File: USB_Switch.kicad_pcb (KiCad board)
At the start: 2 copper layers, 42 x 61 mm, 30 parts, among them J1 Conn_01x06, J2 USB_IN, J3 USB_OUT, J4 Conn_01x08, J5 USB_OUT, Q1 Q_NMOS_GDS, Q2 Q_NMOS_GDS, SW1 PRGM, U1 AMS1117-3.3, U2 INA219AxD, U3 INA219AxD, U4 ESP-12F

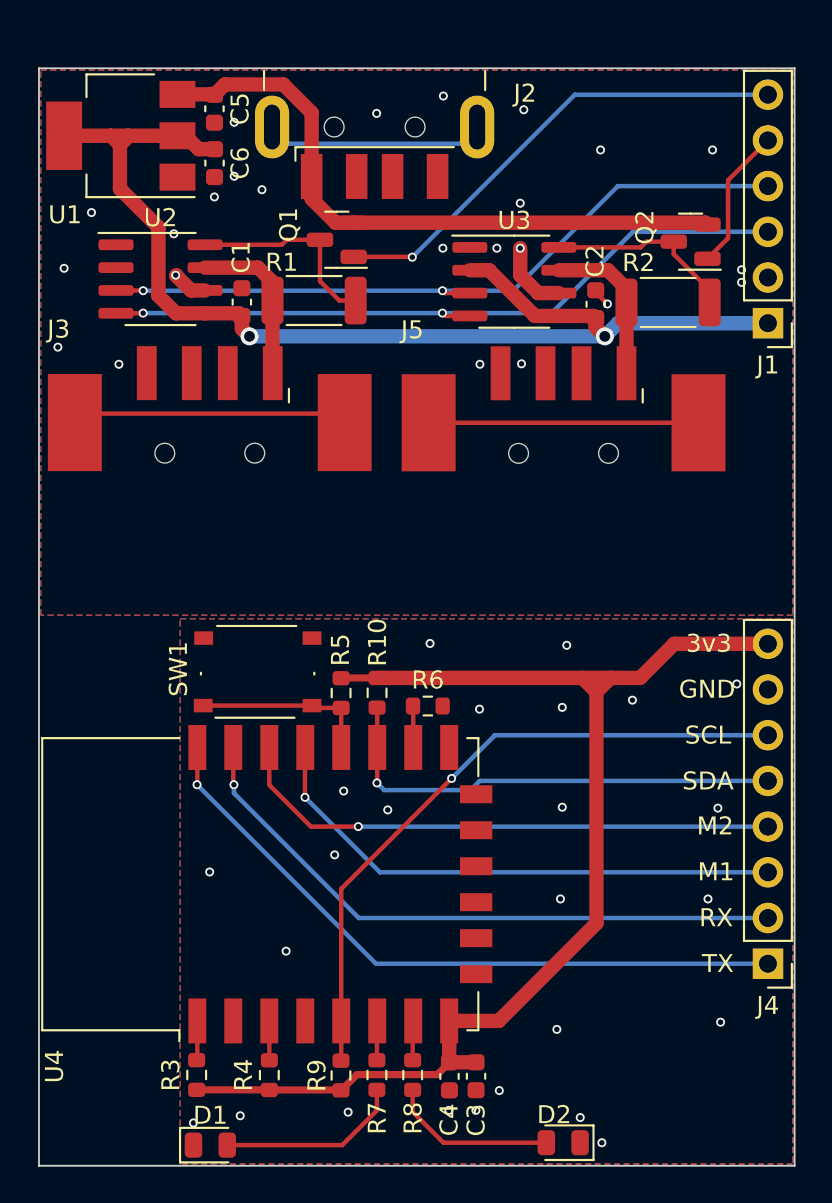
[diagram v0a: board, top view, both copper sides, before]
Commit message: Fixed inversed naming on connectors
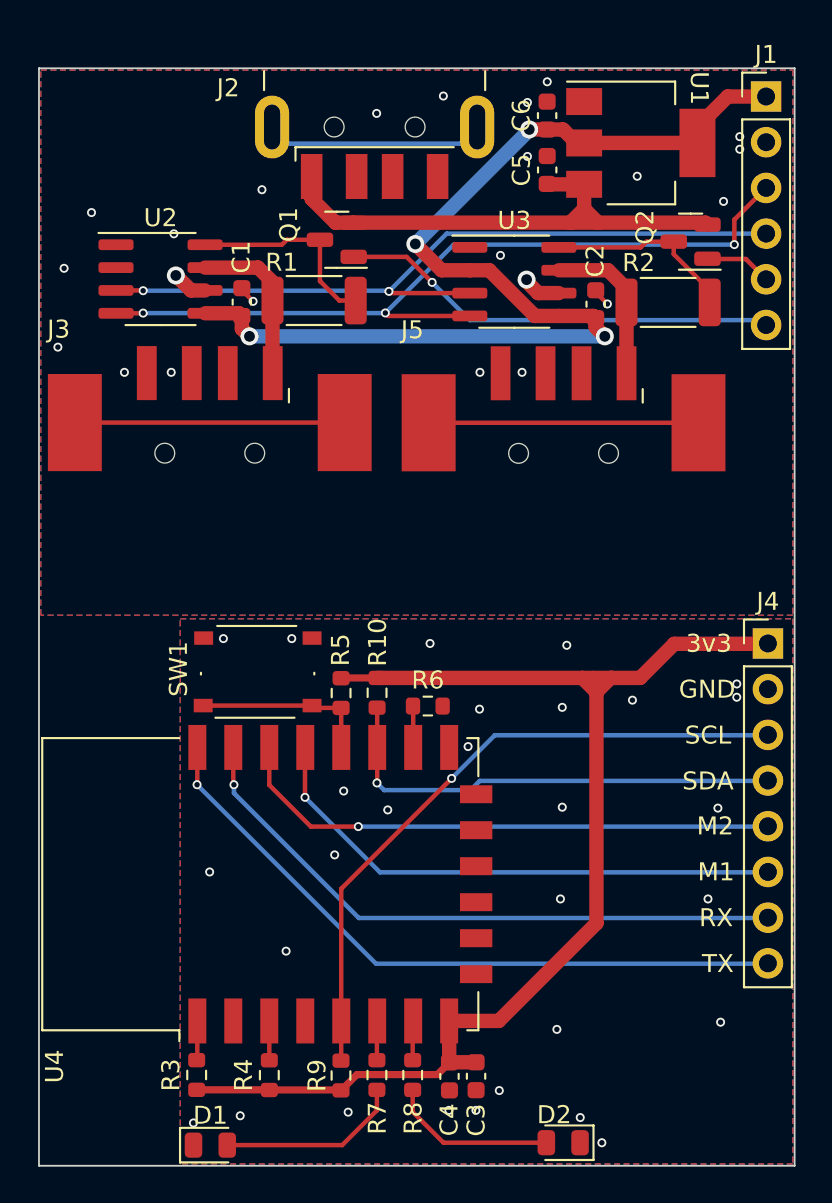
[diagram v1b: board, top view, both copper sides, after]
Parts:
- moved U1 28.9 mm to (69.0, 86.5), turned to 0 degrees
- moved C5 18.8 mm to (63.8, 88.0), turned to 90 degrees
- moved C6 18.7 mm to (63.8, 85.0), turned to 90 degrees
- moved J4 17.8 mm to (76.0, 114.3), turned to 0 degrees
- moved J1 12.6 mm to (76.0, 83.9), turned to 0 degrees
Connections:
- J4 pad 1: /Control Board/C_TX -> /Control Board/C_3v3
- J4 pad 2: /Control Board/C_RX -> GND
- J4 pad 3: /Control Board/M1_TOGGLE -> /Control Board/C_I2C_SCL
- J4 pad 4: /Control Board/M2_TOGGLE -> /Control Board/C_I2C_SDA
- J4 pad 5: /Control Board/C_I2C_SDA -> /Control Board/M2_TOGGLE
- J4 pad 6: /Control Board/C_I2C_SCL -> /Control Board/M1_TOGGLE
- J4 pad 7: GND -> /Control Board/C_RX
- J4 pad 8: /Control Board/C_3v3 -> /Control Board/C_TX
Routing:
- net /MOSFET Board/5V_IN: track 35.7 -> 29.4 mm
- net /MOSFET Board/M_I2C_SCL: track 39.7 -> 44.6 mm, vias 2 -> 3
- net /MOSFET Board/M2_TOGGLE: track 7.97 -> 3.73 mm
- net /MOSFET Board/M_3v3: track 64.2 -> 60.2 mm, vias 2 -> 4
- net /MOSFET Board/M1_TOGGLE: track 26.8 -> 24.5 mm
- net /MOSFET Board/M_I2C_SDA: track 40.2 -> 42.0 mm
- net GND: track 7.06 -> 6.13 mm, vias 49 -> 52

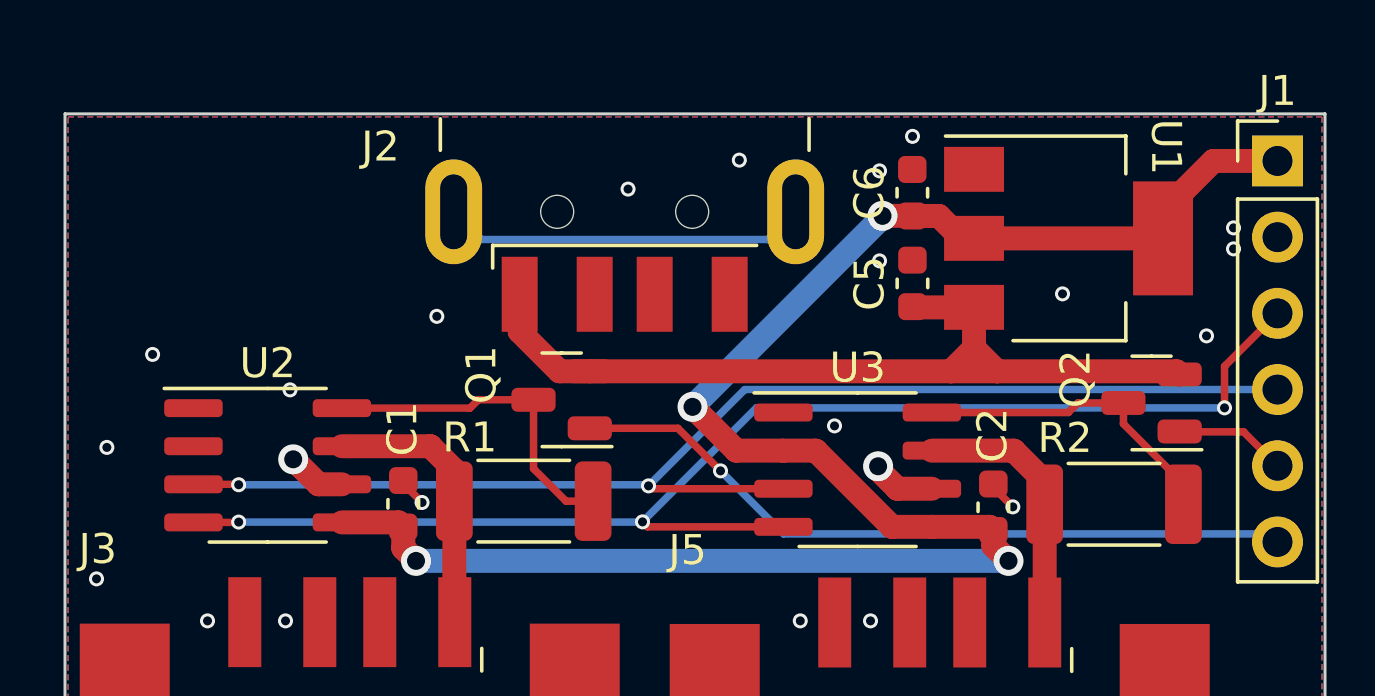
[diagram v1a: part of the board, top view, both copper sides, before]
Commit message: Added more GND vias, fixed incorrect net trace sizing
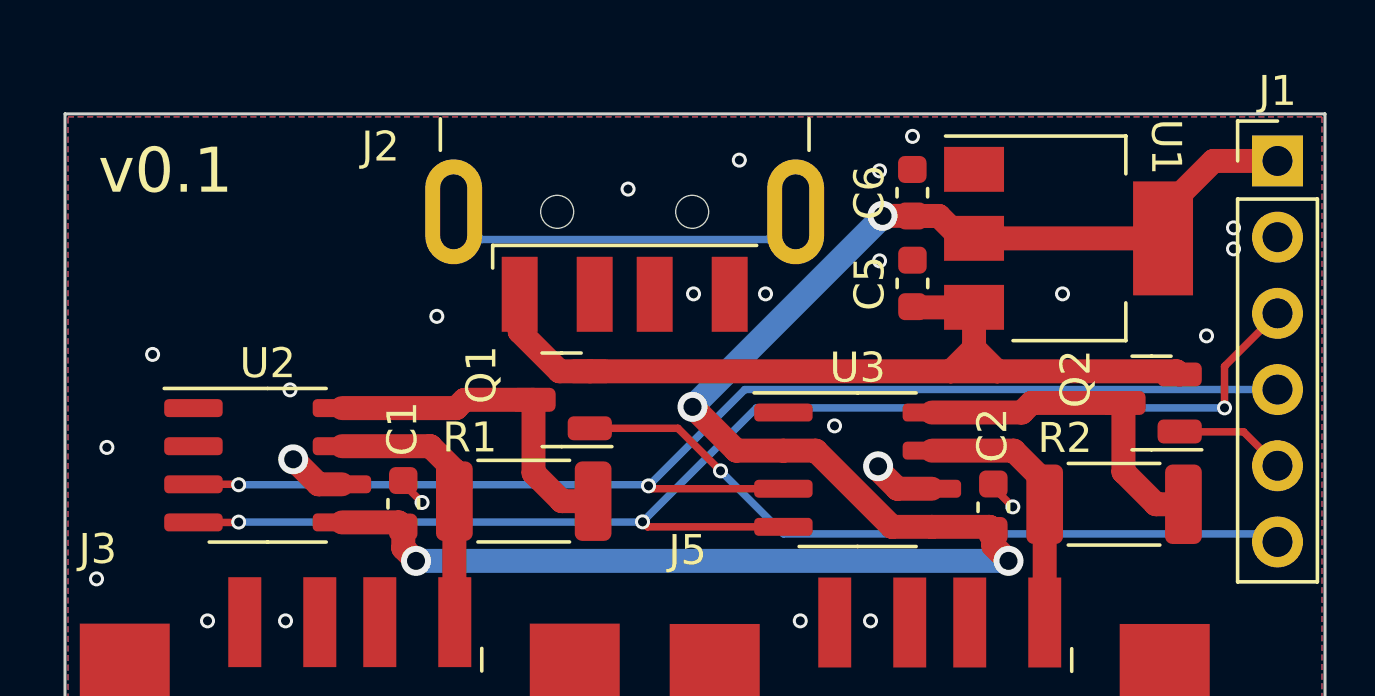
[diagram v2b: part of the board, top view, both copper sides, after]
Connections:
- net Net-(Q1-Pad3) renamed /MOSFET Board/5V_PRER_1
- net Net-(Q2-Pad3) renamed /MOSFET Board/5V_PRER_2
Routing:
- net /MOSFET Board/5V_PRER_2: track 10.7 -> 11.3 mm
- net GND: vias 52 -> 54
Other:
- board text added: "v0.1"
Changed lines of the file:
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@@
   )
   (paper "A4")
+  (title_block
+    (title "Smart USB Port Schematic")
+    (date "2022-10-23")
+    (rev "0.1")
+  )
   (layers
     (0 "F.Cu" signal)
@@
   )
   (net 0 "")
-  (net 1 "Net-(Q1-Pad3)")
+  (net 1 "/MOSFET Board/5V_PRER_1")
   (net 2 "/MOSFET Board/5V_OUT_1")
-  (net 3 "Net-(Q2-Pad3)")
+  (net 3 "/MOSFET Board/5V_PRER_2")
   (net 4 "Net-(R3-Pad2)")
   (net 5 "Net-(R4-Pad2)")
@@
       (net 10 "/MOSFET Board/5V_IN") (pinfunction "D") (pintype "passive"))
     (pad "3" smd roundrect (at 0.9375 0 180) (size 1.475 0.8) (layers "F.Cu" "F.Paste" "F.Mask") (roundrect_rratio 0.25)
-      (net 1 "Net-(Q1-Pad3)") (pinfunction "S") (pintype "passive"))
+      (net 1 "/MOSFET Board/5V_PRER_1") (pinfunction "S") (pintype "passive"))
     (model "${KICAD6_3DMODEL_DIR}/Package_TO_SOT_SMD.3dshapes/SOT-23.wrl"
       (offset (xyz 0 0 0))
@@
       (net 10 "/MOSFET Board/5V_IN") (pinfunction "D") (pintype "passive"))
     (pad "3" smd roundrect (at 0.9375 0 180) (size 1.475 0.8) (layers "F.Cu" "F.Paste" "F.Mask") (roundrect_rratio 0.25)
-      (net 3 "Net-(Q2-Pad3)") (pinfunction "S") (pintype "passive"))
+      (net 3 "/MOSFET Board/5V_PRER_2") (pinfunction "S") (pintype "passive"))
     (model "${KICAD6_3DMODEL_DIR}/Package_TO_SOT_SMD.3dshapes/SOT-23.wrl"
       (offset (xyz 0 0 0))
@@
     (fp_line (start -2.5 -1.25) (end 2.5 -1.25) (layer "F.Fab") (width 0.1))
     (pad "1" smd roundrect (at -2.3125 0 180) (size 1.225 2.65) (layers "F.Cu" "F.Paste" "F.Mask") (roundrect_rratio 0.204082)
-      (net 3 "Net-(Q2-Pad3)") (pintype "passive"))
+      (net 3 "/MOSFET Board/5V_PRER_2") (pintype "passive"))
     (pad "2" smd roundrect (at 2.3125 0 180) (size 1.225 2.65) (layers "F.Cu" "F.Paste" "F.Mask") (roundrect_rratio 0.204082)
       (net 38 "/MOSFET Board/5V_OUT_2") (pintype "passive"))
@@
       (net 2 "/MOSFET Board/5V_OUT_1") (pinfunction "IN-") (pintype "input"))
     (pad "8" smd roundrect (at 2.475 -1.905) (size 1.95 0.6) (layers "F.Cu" "F.Paste" "F.Mask") (roundrect_rratio 0.25)
-      (net 1 "Net-(Q1-Pad3)") (pinfunction "IN+") (pintype "input"))
+      (net 1 "/MOSFET Board/5V_PRER_1") (pinfunction "IN+") (pintype "input"))
     (model "${KICAD6_3DMODEL_DIR}/Package_SO.3dshapes/SOIC-8_3.9x4.9mm_P1.27mm.wrl"
       (offset (xyz 0 0 0))
@@
     (fp_line (start 2.5 -1.25) (end 2.5 1.25) (layer "F.Fab") (width 0.1))
     (pad "1" smd roundrect (at -2.3125 0 180) (size 1.225 2.65) (layers "F.Cu" "F.Paste" "F.Mask") (roundrect_rratio 0.204082)
-      (net 1 "Net-(Q1-Pad3)") (pintype "passive"))
+      (net 1 "/MOSFET Board/5V_PRER_1") (pintype "passive"))
     (pad "2" smd roundrect (at 2.3125 0 180) (size 1.225 2.65) (layers "F.Cu" "F.Paste" "F.Mask") (roundrect_rratio 0.204082)
       (net 2 "/MOSFET Board/5V_OUT_1") (pintype "passive"))
@@
       (net 38 "/MOSFET Board/5V_OUT_2") (pinfunction "IN-") (pintype "input"))
     (pad "8" smd roundrect (at 2.475 -1.905) (size 1.95 0.6) (layers "F.Cu" "F.Paste" "F.Mask") (roundrect_rratio 0.25)
-      (net 3 "Net-(Q2-Pad3)") (pinfunction "IN+") (pintype "input"))
+      (net 3 "/MOSFET Board/5V_PRER_2") (pinfunction "IN+") (pintype "input"))
     (model "${KICAD6_3DMODEL_DIR}/Package_SO.3dshapes/SOIC-8_3.9x4.9mm_P1.27mm.wrl"
       (offset (xyz 0 0 0))
@@
     (effects (font (size 1 1) (thickness 0.15)))
   )
+  (gr_text "v0.1" (at 38.8836 84.2304) (layer "F.SilkS")
+    (effects (font (size 1.5 1.5) (thickness 0.3)))
+  )
   (gr_text "M1" (at 73.168794 127.001606) (layer "F.SilkS")
     (effects (font (size 1 1) (thickness 0.15)))
@@
     (effects (font (size 1 1) (thickness 0.15)))
   )
-  (segment (start 49.0328 92.139) (end 49.3098 91.862) (width 0.25) (layer "F.Cu") (net 1))
-  (segment (start 51.1507 94.1579) (end 52.233 95.2402) (width 0.25) (layer "F.Cu") (net 1))
-  (segment (start 44.7646 92.139) (end 49.0328 92.139) (width 0.25) (layer "F.Cu") (net 1))
-  (segment (start 49.3098 91.862) (end 51.1507 91.862) (width 0.25) (layer "F.Cu") (net 1))
-  (segment (start 52.233 95.2402) (end 53.1373 95.2402) (width 0.25) (layer "F.Cu") (net 1))
-  (segment (start 51.1507 91.862) (end 51.1507 94.1579) (width 0.25) (layer "F.Cu") (net 1))
+  (segment (start 48.852 91.862) (end 51.1507 91.862) (width 0.8) (layer "F.Cu") (net 1))
+  (segment (start 53.1373 95.2402) (end 52.0934 95.2402) (width 0.8) (layer "F.Cu") (net 1))
+  (segment (start 51.1507 94.2975) (end 51.1507 91.862) (width 0.8) (layer "F.Cu") (net 1))
+  (segment (start 52.0934 95.2402) (end 51.1507 94.2975) (width 0.8) (layer "F.Cu") (net 1))
+  (segment (start 48.575 92.139) (end 48.852 91.862) (width 0.8) (layer "F.Cu") (net 1))
+  (segment (start 44.7646 92.139) (end 48.575 92.139) (width 0.8) (layer "F.Cu") (net 1))
   (segment (start 47.7122 93.409) (end 44.7646 93.409) (width 0.8) (layer "F.Cu") (net 2))
   (segment (start 48.5123 95.2402) (end 48.5123 94.2091) (width 0.8) (layer "F.Cu") (net 2))
@@
   (segment (start 48.5123 95.2402) (end 48.5123 99.2597) (width 0.8) (layer "F.Cu") (net 2))
   (segment (start 48.5123 99.2597) (end 48.5256 99.273) (width 0.8) (layer "F.Cu") (net 2))
-  (segment (start 70.8141 92.6631) (end 72.8141 94.6631) (width 0.25) (layer "F.Cu") (net 3))
-  (segment (start 68.9768 92.2864) (end 69.2962 91.967) (width 0.25) (layer "F.Cu") (net 3))
-  (segment (start 69.2962 91.967) (end 70.8141 91.967) (width 0.25) (layer "F.Cu") (net 3))
-  (segment (start 64.4294 92.2864) (end 68.9768 92.2864) (width 0.25) (layer "F.Cu") (net 3))
-  (segment (start 70.8141 91.967) (end 70.8141 92.6631) (width 0.25) (layer "F.Cu") (net 3))
-  (segment (start 72.8141 94.6631) (end 72.8141 95.3434) (width 0.25) (layer "F.Cu") (net 3))
+  (segment (start 71.8966 95.3434) (end 72.8141 95.3434) (width 0.8) (layer "F.Cu") (net 3))
+  (segment (start 70.8141 94.2609) (end 71.8966 95.3434) (width 0.8) (layer "F.Cu") (net 3))
+  (segment (start 70.8141 91.967) (end 70.8141 94.2609) (width 0.8) (layer "F.Cu") (net 3))
+  (segment (start 64.4294 92.2864) (end 67.4276 92.2864) (width 0.8) (layer "F.Cu") (net 3))
+  (segment (start 67.4276 92.2864) (end 67.747 91.967) (width 0.8) (layer "F.Cu") (net 3))
+  (segment (start 67.747 91.967) (end 70.8141 91.967) (width 0.8) (layer "F.Cu") (net 3))
   (segment (start 44.3336 135.2804) (end 44.3336 137.4238) (width 0.25) (layer "F.Cu") (net 4))
   (segment (start 44.3336 137.4238) (end 44.2978 137.4596) (width 0.25) (layer "F.Cu") (net 4))
@@
   (via (at 74.4836 86.8304) (size 0.5) (drill 0.3) (layers "F.Cu" "B.Cu") (free) (net 27))
   (via (at 74.4836 86.1304) (size 0.5) (drill 0.3) (layers "F.Cu" "B.Cu") (free) (net 27))
+  (via (at 56.4836 88.3304) (size 0.5) (drill 0.3) (layers "F.Cu" "B.Cu") (free) (net 27))
   (via (at 44.118794 140.951606) (size 0.5) (drill 0.3) (layers "F.Cu" "B.Cu") (free) (net 27))
   (via (at 59.818794 140.251606) (size 0.5) (drill 0.3) (layers "F.Cu" "B.Cu") (free) (net 27))
@@
   (via (at 64.868794 114.401606) (size 0.5) (drill 0.3) (layers "F.Cu" "B.Cu") (free) (net 27))
   (via (at 74.318087 117.288769) (size 0.5) (drill 0.3) (layers "F.Cu" "B.Cu") (free) (net 27))
+  (via (at 58.8836 88.3304) (size 0.5) (drill 0.3) (layers "F.Cu" "B.Cu") (free) (net 27))
   (via (at 72.718794 128.501606) (size 0.5) (drill 0.3) (layers "F.Cu" "B.Cu") (free) (net 27))
   (via (at 64.618794 123.401606) (size 0.5) (drill 0.3) (layers "F.Cu" "B.Cu") (free) (net 27))
